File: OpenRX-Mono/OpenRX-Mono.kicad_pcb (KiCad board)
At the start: 6 copper layers, 10 x 14.2 mm, 48 parts, among them T1 0900PC16J0042001E, U1 ESP32-C3FH4, U2 TLV75533PDQNR, U3 TS2306A 240GF MSM 9_C2976675, U4 LR1121IMLTRT, U5 OW7EL89CENUYO3YLC-32M, U7 RFX2401C, U8 SKY13414-485LF, X1 CJ17-400001010B20

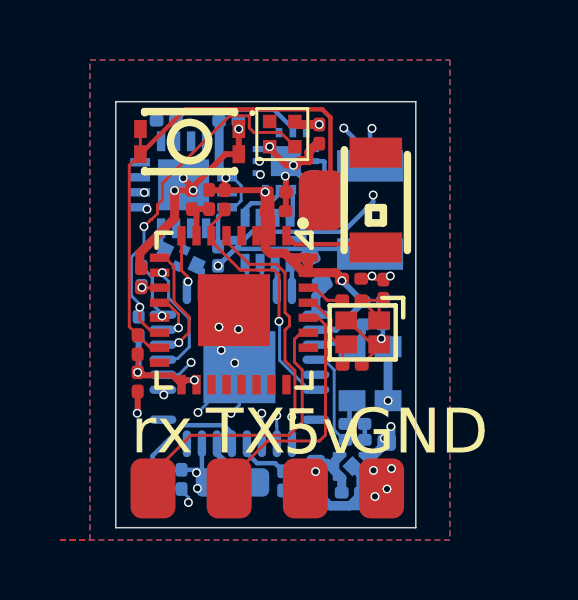
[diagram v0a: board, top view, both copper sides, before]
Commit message: switch to 0.2mm vias
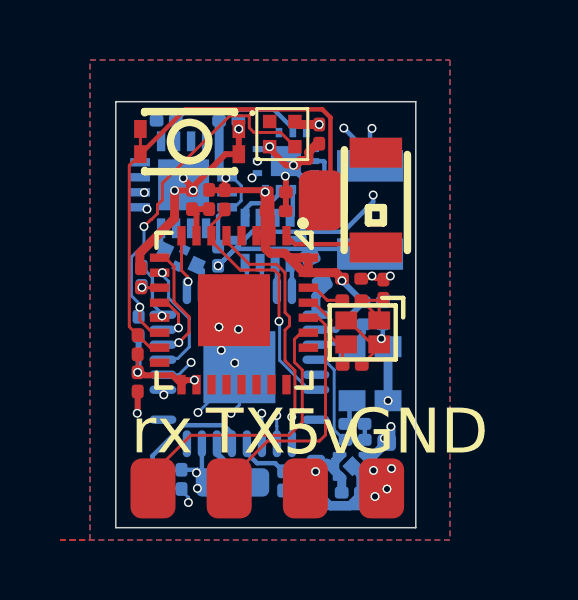
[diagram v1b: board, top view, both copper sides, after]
